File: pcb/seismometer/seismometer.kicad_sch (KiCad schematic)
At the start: 14 parts

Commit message: Pi Pico Schematic
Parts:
- added C? (x4): 10uF, symbol Device:C
- added C?: 1000uF, symbol Device:C_Polarized
- added Q?: DMG2305UX-13, digikey-footprints:SOT-23-3, symbol dk_Transistors-FETs-MOSFETs-Single:DMG2305UX-13
- added R?: 100R, symbol Device:R
- added SW?: Reset, symbol Switch:SW_Push
- added U?: Pico, RPi_Pico:RPi_Pico_SMD_TH, symbol MCU_RaspberryPi_and_Boards:Pico
- added U?: LM4040DBZ-3, Package_TO_SOT_SMD:SOT-23, symbol Reference_Voltage:LM4040DBZ-3
- added U?: LM1117-3.3, symbol Regulator_Linear:LM1117-3.3
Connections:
- net +3.3V: now also C?.1, C?.1, R?.1, U?.2 (VO); no longer RV?.1, RV?.3
- net GND: now also C?.2, C?.2, C?.2, C?.2, C?.2, SW?.2, U?.1 (GND), U?.13 (GND), U?.18 (GND), U?.2 (A), U?.23 (GND), U?.28 (GND), U?.3 (GND), U?.33 (AGND), U?.38 (GND), U?.42 (GND), U?.8 (GND)
- net Pendulum 100x: now also U?.32 (GPIO27_ADC1)
- net Pendulum 10x: now also U?.31 (GPIO26_ADC0)
- new net: SW?.1, U?.30 (RUN)
- new net +VDC: Q?.3 (D)
- new net I2C SCL: U?.7 (GPIO5)
- new net I2C SDA: U?.6 (GPIO4)
- new net UART RX: U?.2 (GPIO1)
- new net UART TX: U?.1 (GPIO0)
- new net V ADC: C?.1, R?.2, RV?.1, RV?.3, U?.1 (K)
- new net V SYS: C?.1, C?.1, Q?.2 (S), U?.3 (VI), U?.39 (VSYS)
- new net VBUS: Q?.1 (G), U?.40 (VBUS)

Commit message: Updating PCB Schematic
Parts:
- added C?: 0.1uF, symbol Device:C
- added C? (x2): 10uF, symbol Device:C
- added C?: 1uF, symbol Device:C
- added J?: GPIO Breakout, symbol Connector_Generic:Conn_02x06_Odd_Even
- added J?: SPI Breakout, symbol Connector_Generic:Conn_02x06_Odd_Even
- added J?: Battery, symbol Connector_Generic:Conn_01x02
- added J?: UART, symbol Connector_Generic:Conn_01x04
- added J?: I2C Breakout, symbol Connector_Generic:Conn_02x04_Odd_Even
- added J?: Micro_SD_Card_Det, symbol Connector:Micro_SD_Card_Det
- added J?: Power, symbol Connector_Generic:Conn_01x02
- added JP?: SolderJumper_2_Bridged, symbol Jumper:SolderJumper_2_Bridged
- added R? (x5): R, symbol Device:R
- added R? (x2): 4.7k, symbol Device:R
- added RN?: R_Network04_US, Resistor_THT:R_Array_SIP5, symbol Device:R_Network04_US
- added RN?: R_Network06_US, Resistor_THT:R_Array_SIP7, symbol Device:R_Network06_US
- added U?: MPU-6500, QFN40P300X300X95-25N, symbol MPU-6500:MPU-6500
- added U?: AT24CS32-SSHM, Package_SO:SOIC-8_3.9x4.9mm_P1.27mm, symbol Memory_EEPROM:AT24CS32-SSHM
- added U?: DS3231M, Package_SO:SOIC-16W_7.5x10.3mm_P1.27mm, symbol Timer_RTC:DS3231M
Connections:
- net +3.3V: now also C?.1, J?.1 (Pin_1), J?.1 (Pin_1), J?.1 (Pin_1), J?.2 (Pin_2), J?.2 (Pin_2), J?.3 (Pin_3), J?.4 (Pin_4), J?.4 (VDD), R?.1, R?.1, R?.1, R?.2, RN?.1 (common), U?.2 (VCC), U?.8 (VCC)
- net +VDC: now also J?.1 (Pin_1)
- net GND: now also C?.2, C?.2, C?.2, C?.2, J?.11 (Pin_11), J?.11 (Pin_11), J?.11 (SHIELD), J?.12 (Pin_12), J?.12 (Pin_12), J?.2 (Pin_2), J?.2 (Pin_2), J?.4 (Pin_4), J?.6 (VSS), J?.7 (Pin_7), J?.8 (Pin_8), U?.10 (GND), U?.11 (FSYNC), U?.11 (GND), U?.12 (GND), U?.13 (GND), U?.18 (GND), U?.20 (RESV_2), U?.4 (GND), U?.5 (GND), U?.6 (GND), U?.7 (GND), U?.7 (WP), U?.8 (GND), U?.9 (GND)
- net I2C SCL: now also J?.5 (Pin_5), J?.6 (Pin_6), R?.2, U?.16 (SCL), U?.23 (SCL/SCLK), U?.6 (SCL)
- net I2C SDA: now also J?.3 (Pin_3), J?.4 (Pin_4), R?.2, U?.15 (SDA), U?.24 (SDA/SDI), U?.5 (SDA)
- net UART RX: now also J?.3 (Pin_3)
- net UART TX: now also J?.2 (Pin_2)
- net V SYS: now also J?.1 (Pin_1), J?.2 (Pin_2)
- net GPIO8: now reaches U?.11 (GPIO8)
- net GPIO8: now also J?.5 (Pin_5)
- net GPIO9: now reaches U?.12 (GPIO9)
- net GPIO9: now also J?.7 (Pin_7)
- net GPIO10: now reaches U?.14 (GPIO10)
- net GPIO10: now also J?.9 (Pin_9)
- net GPIO11: now reaches U?.15 (GPIO11)
- net GPIO11: now also J?.6 (Pin_6)
- net GPIO12: now reaches U?.16 (GPIO12)
- net GPIO12: now also J?.8 (Pin_8)
- net SPI0 CS A: now reaches U?.17 (GPIO13)
- net SPI0 CS A: now also J?.3 (Pin_3)
- net SPI0 CS B: now reaches U?.19 (GPIO14)
- net SPI0 CS B: now also J?.4 (Pin_4)
- net SD0 CS: now reaches U?.20 (GPIO15)
- net SD0 CS: now also J?.2 (DAT3/CD), RN?.3 (R2)
- net SPI0 RX: now reaches U?.21 (GPIO16)
- net SPI0 RX: now also J?.7 (DAT0), J?.7 (Pin_7), J?.8 (Pin_8), R?.2, RN?.6 (R5)
- net SPI0 SCK: now reaches U?.24 (GPIO18)
- net SPI0 SCK: now also J?.5 (CLK), J?.5 (Pin_5), J?.6 (Pin_6), RN?.5 (R4)
- net SPI0 TX: now reaches U?.25 (GPIO19)
- net SPI0 TX: now also J?.10 (Pin_10), J?.3 (CMD), J?.9 (Pin_9), RN?.4 (R3)
- net SD0 CD: now reaches U?.26 (GPIO20)
- net SD0 CD: now also J?.10 (DET_A), J?.9 (DET_B), R?.2
- net Peripheral EN: now reaches U?.27 (GPIO21)
- net RTC SQW: now reaches U?.29 (GPIO22)
- net RTC SQW: now also R?.2, U?.3 (~{INT}/SQW)
- net RESET: now reaches SW?.1, U?.30 (RUN)
- net RESET: now also JP?.1 (A)
- net ADC2: now reaches U?.34 (GPIO28_ADC2)
- net ADC2: now also J?.10 (Pin_10)
- new net: RN?.3 (R2), U?.3 (A2)
- new net: RN?.4 (R3), U?.2 (A1)
- new net: RN?.5 (R4), U?.1 (A0)
- new net: C?.1, U?.10 (REGOUT)
- new net: R?.1, U?.9 (AD0/SDO)
- new net: R?.1, U?.1 (32KHZ)
- new net: JP?.2 (B), U?.4 (~{RST})
- new net +3V3: C?.1, C?.1, R?.1, R?.1, R?.2, RN?.1 (common), U?.13 (VDD), U?.22 (NCS), U?.8 (VDDIO)
- new net +BATT: J?.1 (Pin_1), U?.14 (VBAT)
- new net Accel INT: U?.12 (INT)
- new net SD0 DAT1: J?.8 (DAT1), RN?.7 (R6)
- new net SD0 DAT2: J?.1 (DAT2), RN?.2 (R1)
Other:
- moved on the sheet: C?, J?, Q?, R?, RV?, SW?, TP?, U?, U?A, U?B, U?C

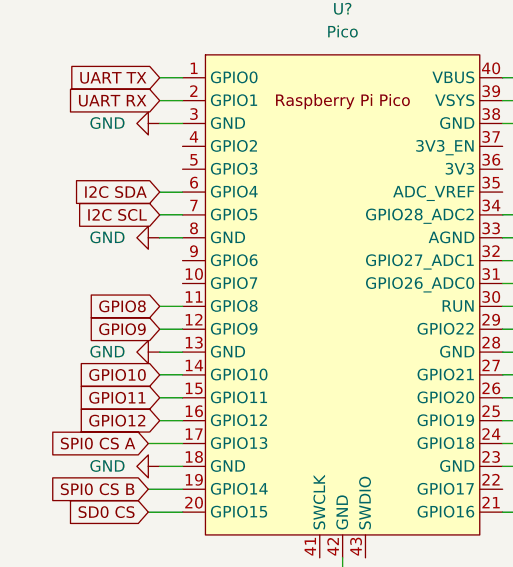
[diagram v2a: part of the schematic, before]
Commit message: Accelerometer Interrupt Pin
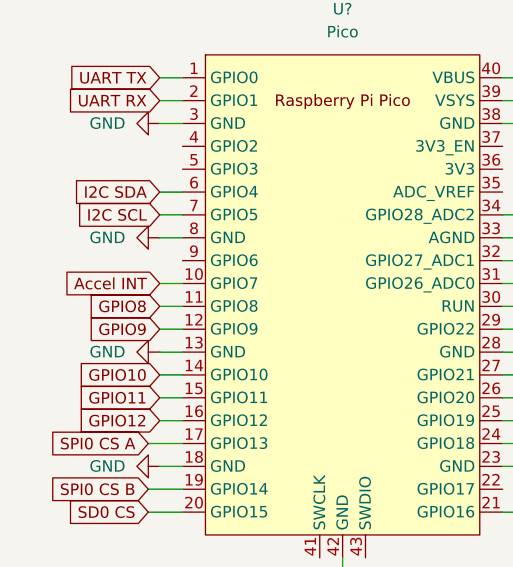
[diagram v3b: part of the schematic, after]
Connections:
- net Accel INT: now also U?.10 (GPIO7)
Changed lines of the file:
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@@
+    (stroke (width 0) (type default) (color 0 0 0 0))
+  )
+  (wire (pts (xy 27.94 50.8) (xy 30.48 50.8))
     (stroke (width 0) (type default) (color 0 0 0 0))
   )
@@
       (effects (font (size 1.27 1.27)) (justify right) hide)
     )
+  )
+  (global_label "Accel INT" (shape input) (at 27.94 50.8 180) (fields_autoplaced)
+    (effects (font (size 1.27 1.27)) (justify right))
+    (property "Intersheet References" "${INTERSHEET_REFS}" (id 0) (at 16.6369 50.8794 0)
+      (effects (font (size 1.27 1.27)) (justify right) hide)
+    )

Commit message: Updating PCB Schematic
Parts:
- removed C? (x3): 10uF, symbol Device:C
- removed J?: GPIO Breakout, symbol Connector_Generic:Conn_02x06_Odd_Even
- removed J?: Pendulum Solenoid, symbol Connector:Conn_01x02_Male
- removed J?: Micro_SD_Card_Det, symbol Connector:Micro_SD_Card_Det
- removed R? (x2): 1k, symbol Device:R
- removed R? (x2): 4.7k, symbol Device:R
- removed R? (x2): 10k, symbol Device:R
- removed RN?: R_Network04_US, Resistor_THT:R_Array_SIP5, symbol Device:R_Network04_US
- removed RN?: R_Network06_US, Resistor_THT:R_Array_SIP7, symbol Device:R_Network06_US
- removed RV?: 1M, symbol Device:R_Potentiometer
- removed RV?: 100k, symbol Device:R_Potentiometer
- removed TP?: Pendulum Raw, symbol Connector:TestPoint_Probe
- removed TP?: Pendulum 10x, symbol Connector:TestPoint_Probe
- removed TP?: Pendulum 100x, symbol Connector:TestPoint_Probe
- removed U? (x3): LM358, symbol Amplifier_Operational:LM358
- added J?: Conn_02x07_Odd_Even, symbol Connector_Generic:Conn_02x07_Odd_Even
- added RN?: R_Pack04, symbol Device:R_Pack04
- added U?: Si7021-A20, Package_DFN_QFN:DFN-6-1EP_3x3mm_P1mm_EP1.5x2.4mm, symbol Sensor_Humidity:Si7021-A20
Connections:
- net +3.3V: now also J?.3 (Pin_3), J?.4 (Pin_4), RN?.5 (R4.2), RN?.6 (R3.2), RN?.7 (R2.2), U?.5 (VDD)
- net ADC2: now also J?.10 (Pin_10), J?.6 (Pin_6), J?.8 (Pin_8)
- net GND: now also J?.13 (Pin_13), J?.14 (Pin_14), RN?.1 (R1.1), RN?.8 (R1.2), U?.2 (GND)
- net GPIO10: now also J?.9 (Pin_9)
- net GPIO8: now also J?.5 (Pin_5)
- net GPIO9: now also J?.7 (Pin_7)
- net I2C SCL: now also U?.6 (SCL)
- net I2C SDA: now also U?.1 (SDA)
- net V SYS: now also J?.1 (Pin_1), J?.2 (Pin_2)
- net at U?.3 (A2): now also RN?.2 (R2.1)
- net at U?.2 (A1): now also RN?.3 (R3.1)
- net at U?.1 (A0): now also RN?.4 (R4.1)
- net Pendulum 100x renamed ADC1
- net Pendulum 10x renamed ADC0
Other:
- added sheet micro_sd_spi (micro_sd_spi.kicad_sch)
- added sheet solenoid_amplifier (solenoid_amplifier.kicad_sch)
- moved on the sheet: C?, J?, JP?, R?, U?
